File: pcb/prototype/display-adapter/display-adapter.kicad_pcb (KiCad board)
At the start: 2 copper layers, 15.2 x 40.6 mm, 5 parts, among them J1 HEADER-1x08, J2 HEADER-1x02, J3 HEADER-1x02, J4 HEADER-1x03, J5 HEADER-1x05

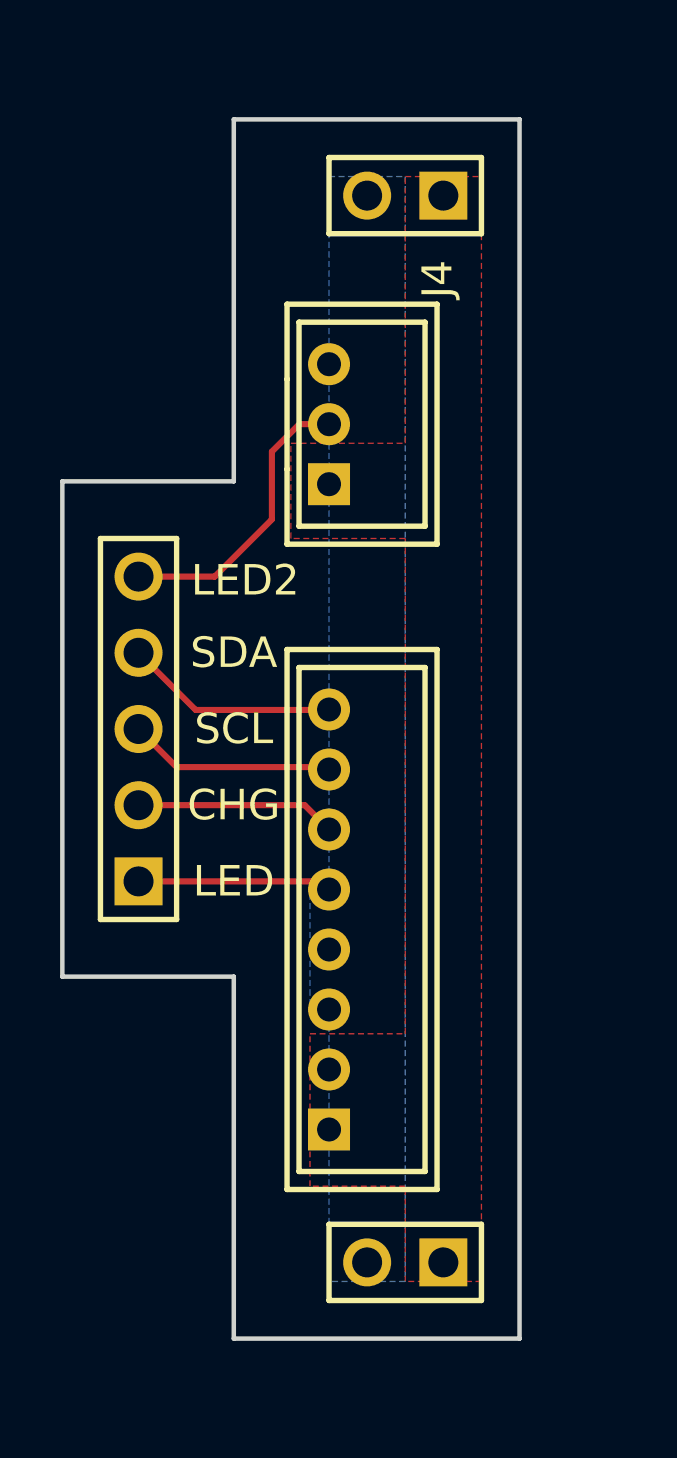
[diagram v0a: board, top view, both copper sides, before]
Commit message: Updated PCB design
+ Completed daughterboard PCB layout.
* Corrected soldermask clerance on front panel pcb.
- Removed input resistor on DIN for RGB lamp board.
* Modified PCB layout for PSU board.
* Updated gerber files.
* Updated schematics pdf, BOM.
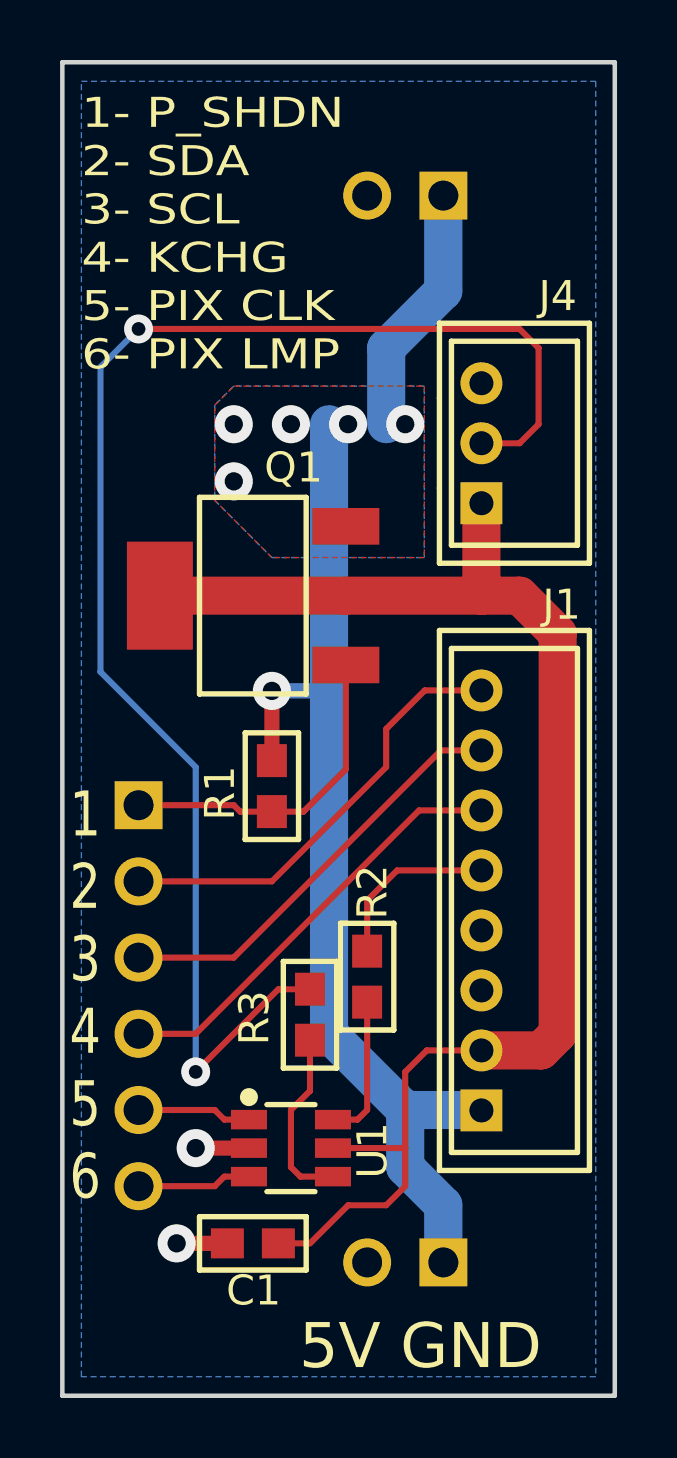
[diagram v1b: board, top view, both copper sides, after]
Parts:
- added C1: 100nF, smt:C-0603, F.Cu at (161.3, 111.1)
- added Q1: NTF6P02, smt-sot:SOT-223, F.Cu at (161.3, 89.5)
- added R1: 10k, smt:R-0603, F.Cu at (161.9, 95.9)
- added R2: 470, smt:R-0603, F.Cu at (165.1, 102.2)
- added R3: 470, smt:R-0603, F.Cu at (163.2, 103.5)
- added U1: SN74LVC2G34DBV, smt-sot:SOT23-6, F.Cu at (162.6, 108.0)
- J1: value HEADER-1x08 -> DISPLAY
- J2, J3: moved to B.Cu
- J4: value HEADER-1x03 -> LAMP
- J5: value HEADER-1x05 -> HEADER-1x06; footprint conn-header:HDR-M-1x05 -> conn-header:HDR-M-1x06; moved to B.Cu
- moved J5 8.89 mm to (157.5, 102.9), turned to 270 degrees
- moved J1 5.12 mm to (168.9, 99.7)
- moved J4 5.12 mm to (168.9, 84.5)
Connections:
- net Net-(J1-Pad7) renamed /SCL
- J1 pad 2: +5V -> /PIX_VCC
- J1 pad 6: Net-(J1-Pad6) -> /KCHG
- J1 pad 8: Net-(J1-Pad8) -> /SDA
- J4 pad 1: +5V -> /PIX_VCC
- J5 pad 1: Net-(J1-Pad5) -> /PIX_SHDN
- J5 pad 2: Net-(J1-Pad6) -> /SDA
- J5 pad 4: Net-(J1-Pad8) -> /KCHG
- J5 pad 5: Net-(J4-Pad2) -> /PIX_CLK
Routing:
- net /PIX_VCC: track 0.00 -> 47.0 mm
- net +5V: track 0.00 -> 44.7 mm, vias 0 -> 6
- net Net-(J4-Pad2): track 9.78 -> 49.9 mm, vias 0 -> 2
- net /SDA: track 0.00 -> 14.8 mm
- net /KCHG: track 0.00 -> 14.5 mm
- net /PIX_SHDN: track 0.00 -> 11.1 mm
- net /SCL: track 6.91 -> 14.3 mm
- net Net-(J1-Pad8): track 7.15 -> 0.00 mm
- net Net-(J1-Pad6): track 6.69 -> 0.00 mm
- net Net-(R3-Pad1): track 0.00 -> 6.02 mm
- net Net-(R2-Pad1): track 0.00 -> 4.87 mm
- net /PIX_LAMP: track 0.00 -> 3.81 mm
- net /PIX_CLK: track 0.00 -> 3.81 mm
- net GND: track 0.00 -> 3.47 mm, vias 0 -> 2
- net Net-(J1-Pad5): track 6.73 -> 5.91 mm
- added copper zone on B.Cu, net +5V
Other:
- board size 15.2 x 40.6 mm -> 18.4 x 44.5 mm
- board text added: "1 2 3 4 5 6"
- board text added: "1- P_SHDN 2- SDA 3- SCL 4- KCHG 5- PIX CLK 6- PIX LMP"
- board text added: "5V GND"
- board text removed: "CHG"
- board text removed: "LED"
- board text removed: "LED2"
- board text removed: "SCL"
- board text removed: "SDA"
